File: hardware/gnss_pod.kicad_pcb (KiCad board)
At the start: 2 copper layers, 89.1 x 92.1 mm, 12 parts, among them J1 SQT-110-01-L-D, J2 SSQ-126-04-G-D, J3 SSQ-126-04-G-D

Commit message: started routing
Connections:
- J1 pad 14: unconnected-(J1-TXD2-Pad14) -> /TX2
- J1 pad 15: unconnected-(J1-RXD2-Pad15) -> /RX2
- J1 pad 3: unconnected-(J1-USB-D-Pad3) -> /USB_N
- J1 pad 4: unconnected-(J1-USB+D+/RXD3-Pad4) -> /USB_P
- J3 pad 35: unconnected-(J3-Pad35) -> /3V3
- J3 pad 36: unconnected-(J3-Pad36) -> /3V3
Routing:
- net /3V3: track 0.00 -> 26.8 mm
- net GNDREF: track 0.42 -> 7.86 mm, vias 0 -> 1
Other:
- board size 89.1 x 92.1 mm -> 89.2 x 92.2 mm

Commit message: new tracks needs review
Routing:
- net /TX1: track 0.00 -> 31.5 mm
- net /RX1: track 0.00 -> 24.2 mm
- net GNDREF: track 7.86 -> 16.4 mm, vias 1 -> 2
- net /3V3: track 26.8 -> 28.3 mm
- added copper zone on B.Cu, net GNDREF

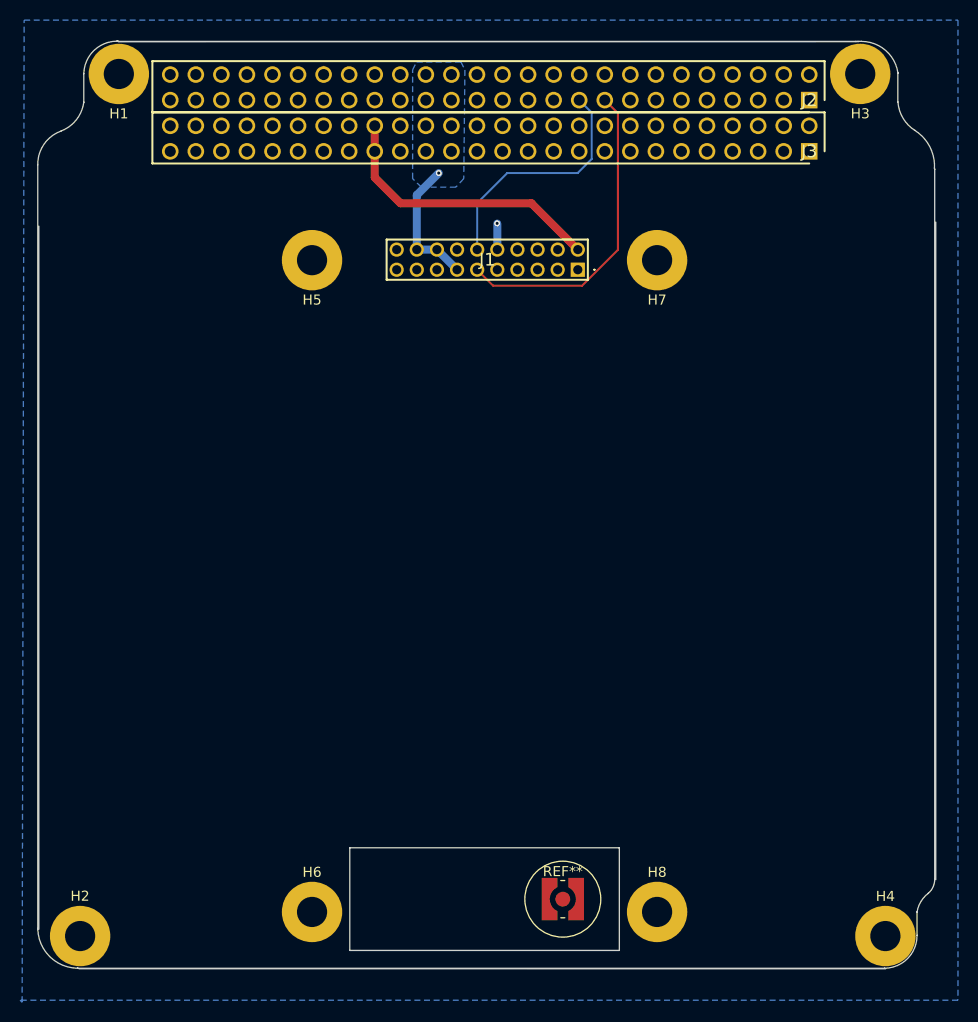
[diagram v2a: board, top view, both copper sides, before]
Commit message: Fixed edge cuts
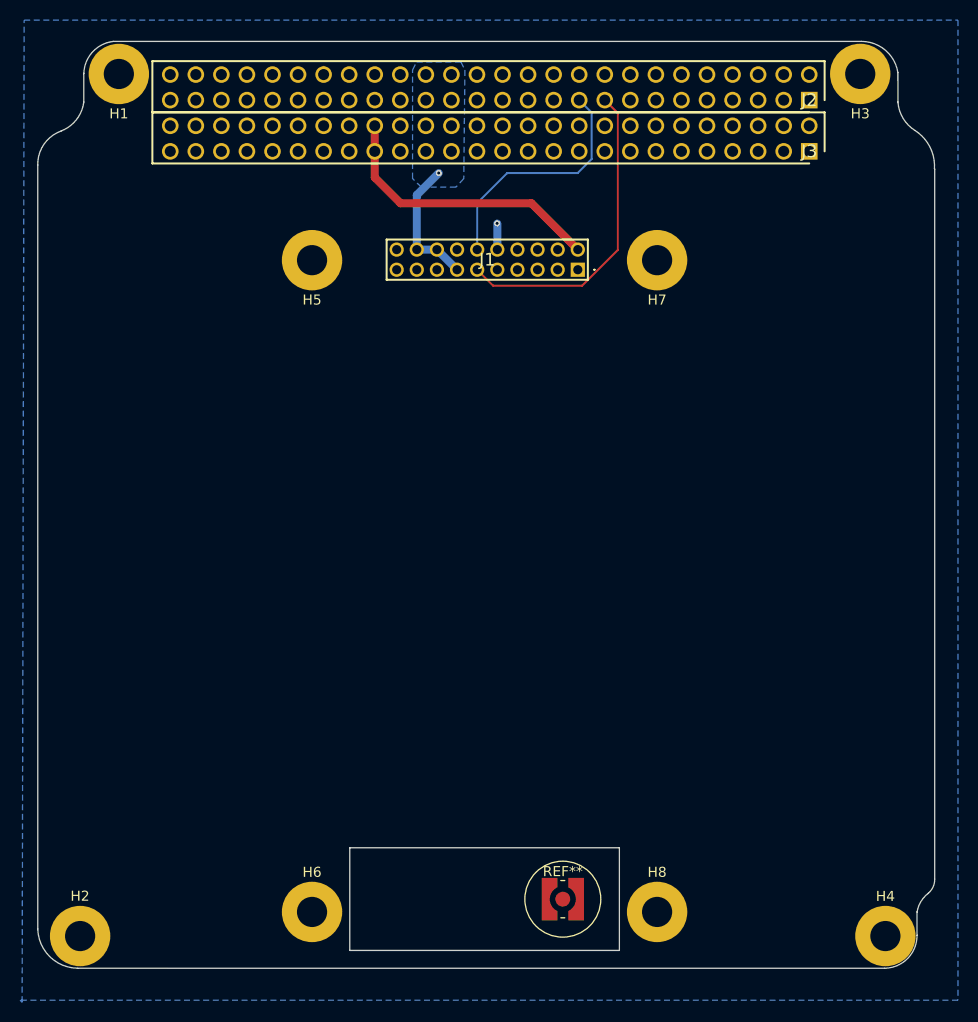
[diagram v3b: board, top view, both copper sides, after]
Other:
- board size 89.2 x 92.2 mm -> 89.1 x 92.1 mm

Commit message: Added CAN Communication
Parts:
- added C1: 0.1uF, Capacitor_SMD:C_0603_1608Metric_Pad1.08x0.95mm_HandSolder, F.Cu at (119.2, 70.3)
- added C2: 22pF, Capacitor_SMD:C_0603_1608Metric_Pad1.08x0.95mm_HandSolder, F.Cu at (121.2, 89.8)
- added C3: 22pF, Capacitor_SMD:C_0603_1608Metric_Pad1.08x0.95mm_HandSolder, F.Cu at (123.6, 94.5)
- added IC1: CDNBS08-PLC03-6, footprints:SOIC127P600X175-8N, F.Cu at (116.4, 92.5)
- added J5: Conn_01x02_Pin, footprints:532614002, F.Cu at (108.1, 92.3)
- added R1: 330, Resistor_SMD:R_0603_1608Metric_Pad0.98x0.95mm_HandSolder, F.Cu at (119.2, 73.7)
- added R2: 120, Resistor_SMD:R_0603_1608Metric_Pad0.98x0.95mm_HandSolder, F.Cu at (121.2, 93.6)
- added U1: TCAN334G, footprints:SOIC127P600X175-8N, F.Cu at (114.2, 70.0)
- J1: footprint gnss_pod_Bib:SQT11001LD -> footprints:SQT11001LD
- J2, J3: footprint gnss_pod_Bib:RHDR52W64P254_2X26_6655X495X864P -> footprints:RHDR52W64P254_2X26_6655X495X864P
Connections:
- net /3V3 renamed VCC
- J1 pad 20: unconnected-(J1-CAN2TX-Pad20) -> /CAN2TX
- J1 pad 8: unconnected-(J1-CAN2RX-Pad8) -> /CAN2RX
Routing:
- added copper zone on F.Cu, net GNDREF
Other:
- board text removed: "PROTOTYPE"

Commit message: need to review the ground plane
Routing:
- net GNDREF: track 16.4 -> 23.1 mm, vias 2 -> 1
- net /RX1: track 24.2 -> 20.2 mm, vias 0 -> 2

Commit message: need to review the ground plane, add vias, make the missing devices connections
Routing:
- net GNDREF: track 23.1 -> 0.45 mm
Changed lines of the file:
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@@
-	)
-	(segment
-		(start 110.281 71.95)
-		(end 111.522 71.95)
-		(width 1)
-		(layer "F.Cu")
-		(net "GNDREF")
-	)
-	(segment
-		(start 110 68.6)
-		(end 110 71.669)
-		(width 1)
-		(layer "F.Cu")
-		(net "GNDREF")
-	)
-	(segment
-		(start 111.522 68.14)
-		(end 110.46 68.14)
-		(width 1)
-		(layer "F.Cu")
-		(net "GNDREF")
-	)
-	(segment
-		(start 116.95 70.68)
-		(end 118.68 70.68)
-		(width 1)
-		(layer "F.Cu")
-		(net "GNDREF")
-	)
-	(segment
-		(start 110.46 68.14)
-		(end 110 68.6)
-		(width 1)
-		(layer "F.Cu")
-		(net "GNDREF")
-	)
-	(segment
-		(start 124.475 92.2625)
-		(end 121.15 88.9375)
-		(width 1)
-		(layer "F.Cu")
-		(net "GNDREF")
 	)
 	(segment
@@
 		(end 143.643438 53.756019)
 		(width 0.254)
-		(layer "F.Cu")
-		(net "GNDREF")
-	)
-	(segment
-		(start 110 71.669)
-		(end 110.281 71.95)
-		(width 1)
-		(layer "F.Cu")
-		(net "GNDREF")
-	)
-	(segment
-		(start 118.68 70.68)
-		(end 119.15 71.15)
-		(width 1)
-		(layer "F.Cu")
-		(net "GNDREF")
-	)
-	(segment
-		(start 124.475 94.55)
-		(end 124.475 92.2625)
-		(width 1)
 		(layer "F.Cu")
 		(net "GNDREF")
@@
 		(end 151 69.2)
 		(width 0.2)
-		(layer "B.Cu")
-		(net "GNDREF")
-	)
-	(segment
-		(start 143.02 71.205)
-		(end 145.02 71.205)
-		(width 1)
-		(layer "B.Cu")
-		(net "GNDREF")
-	)
-	(segment
-		(start 151.02 71.205)
-		(end 151.02 69.22)
-		(width 1)
-		(layer "B.Cu")
-		(net "GNDREF")
-	)
-	(segment
-		(start 145.02 71.205)
-		(end 147.02 73.205)
-		(width 1)
 		(layer "B.Cu")
 		(net "GNDREF")
@@
 	(zone
 		(net "GNDREF")
-		(layer "F.Cu")
+		(layers "F.Cu" "B.Cu")
 		(hatch edge 0.5)
-		(priority 1)
 		(connect_pads
 			(clearance 0)
@@
 		(polygon
 			(pts
-				(xy 112.6 91.8) (xy 113 91.4) (xy 120 91.4) (xy 120.4 90.4) (xy 120.4 88.6) (xy 120.8 88.2) (xy 121.6 88.2)
-				(xy 122 88.6) (xy 122 93) (xy 121.15 93.6125) (xy 113 93.6125) (xy 112.6 93.2)
-			)
-		)
-	)
-	(zone
-		(net "GNDREF")
-		(layers "F.Cu" "B.Cu")
-		(hatch edge 0.5)
-		(connect_pads
-			(clearance 0)
-		)
-		(min_thickness 0.25)
-		(fill yes
-			(thermal_gap 0.5)
-			(thermal_bridge_width 0.5)
-			(island_removal_mode 0)
-		)
-		(polygon
-			(pts
 				(xy 104.2 48.8) (xy 195.299999 48.8) (xy 195.099999 146) (xy 103.8 146)
 			)
@@
 			)
 		)
-	)
-	(zone
-		(net "GNDREF")
-		(layer "B.Cu")
-		(hatch edge 0.5)
-		(priority 2)
-		(connect_pads
-			(clearance 0)
-		)
-		(min_thickness 0.25)
-		(fill yes
-			(thermal_gap 0.5)
-			(thermal_bridge_width 0.5)
-			(island_removal_mode 0)
-		)
-		(polygon
-			(pts
-				(xy 142.8 53.2) (xy 143.2 52.8) (xy 147.2 52.8) (xy 147.6 53.2) (xy 147.6 63) (xy 147.2 63.4) (xy 143.195015 63.395837)
-				(xy 142.8 63)
-			)
-		)
